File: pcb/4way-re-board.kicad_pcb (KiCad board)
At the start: 2 copper layers, 21 x 45.5 mm, 5 parts

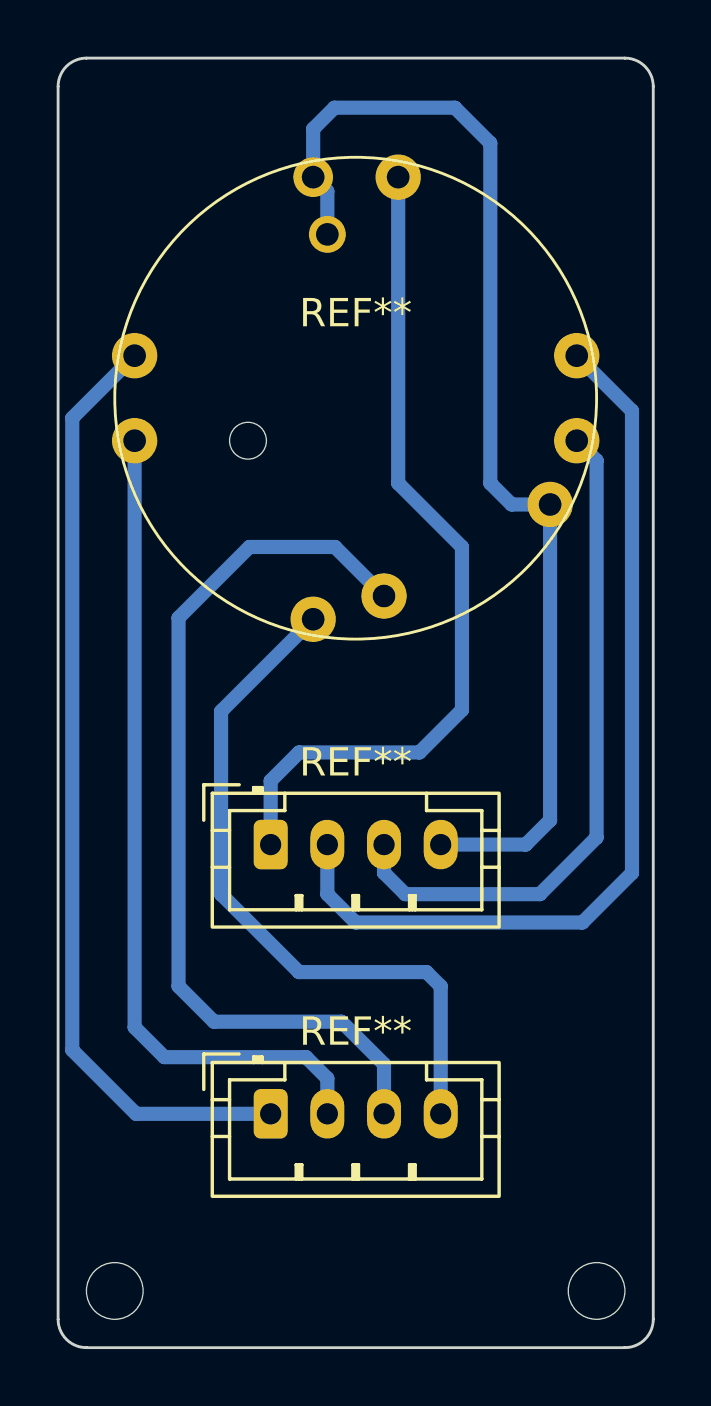
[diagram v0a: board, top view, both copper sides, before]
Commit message: add nc and chenge uf2 for studio
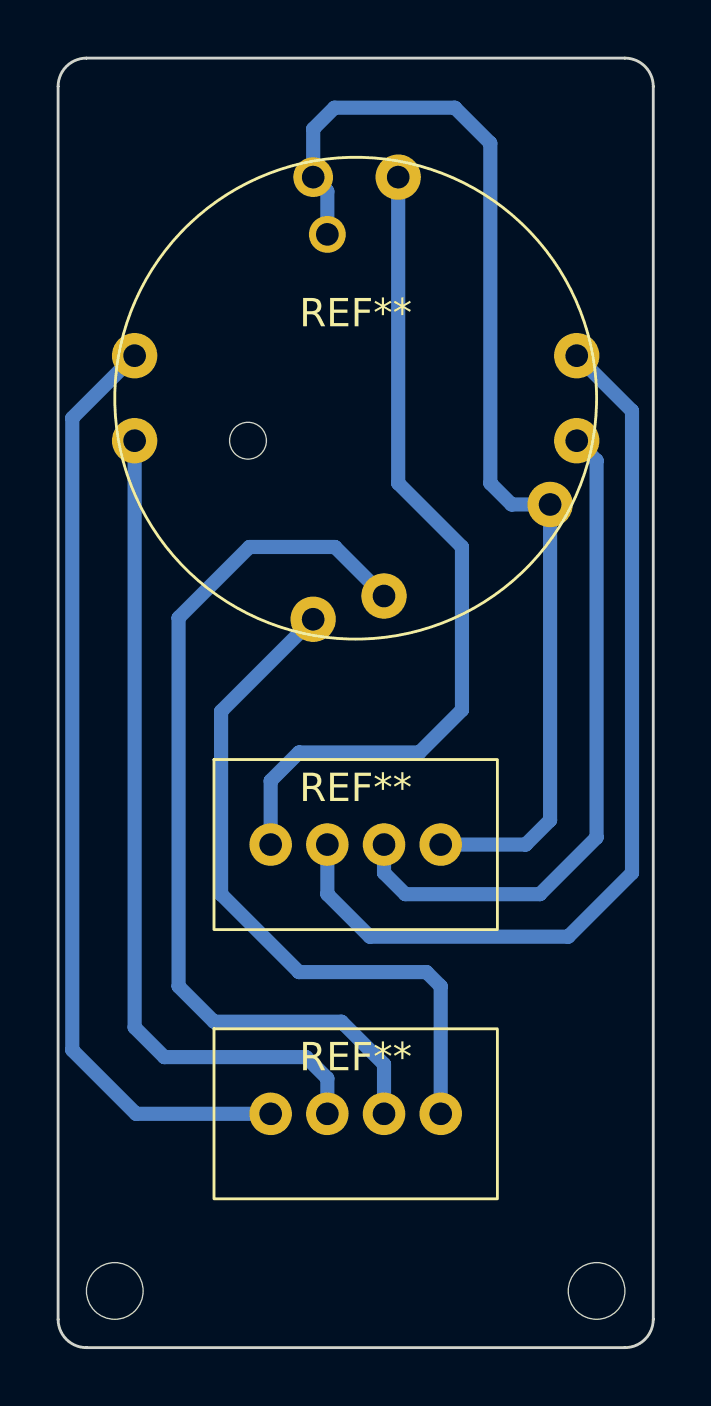
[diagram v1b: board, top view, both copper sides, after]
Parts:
- removed the REF** at (97.0, 101.8)
- removed the REF** at (97.0, 92.2)
- added REF**: JST-PH-2-V, Suzuki:JstPh4Vertical, F.Cu at (100.0, 101.8)
- added REF**: JST-PH-2-V, Suzuki:JstPh4Vertical, F.Cu at (100.0, 92.2)
